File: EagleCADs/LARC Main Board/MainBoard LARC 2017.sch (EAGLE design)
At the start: 31 parts, among them IC1 7805TV

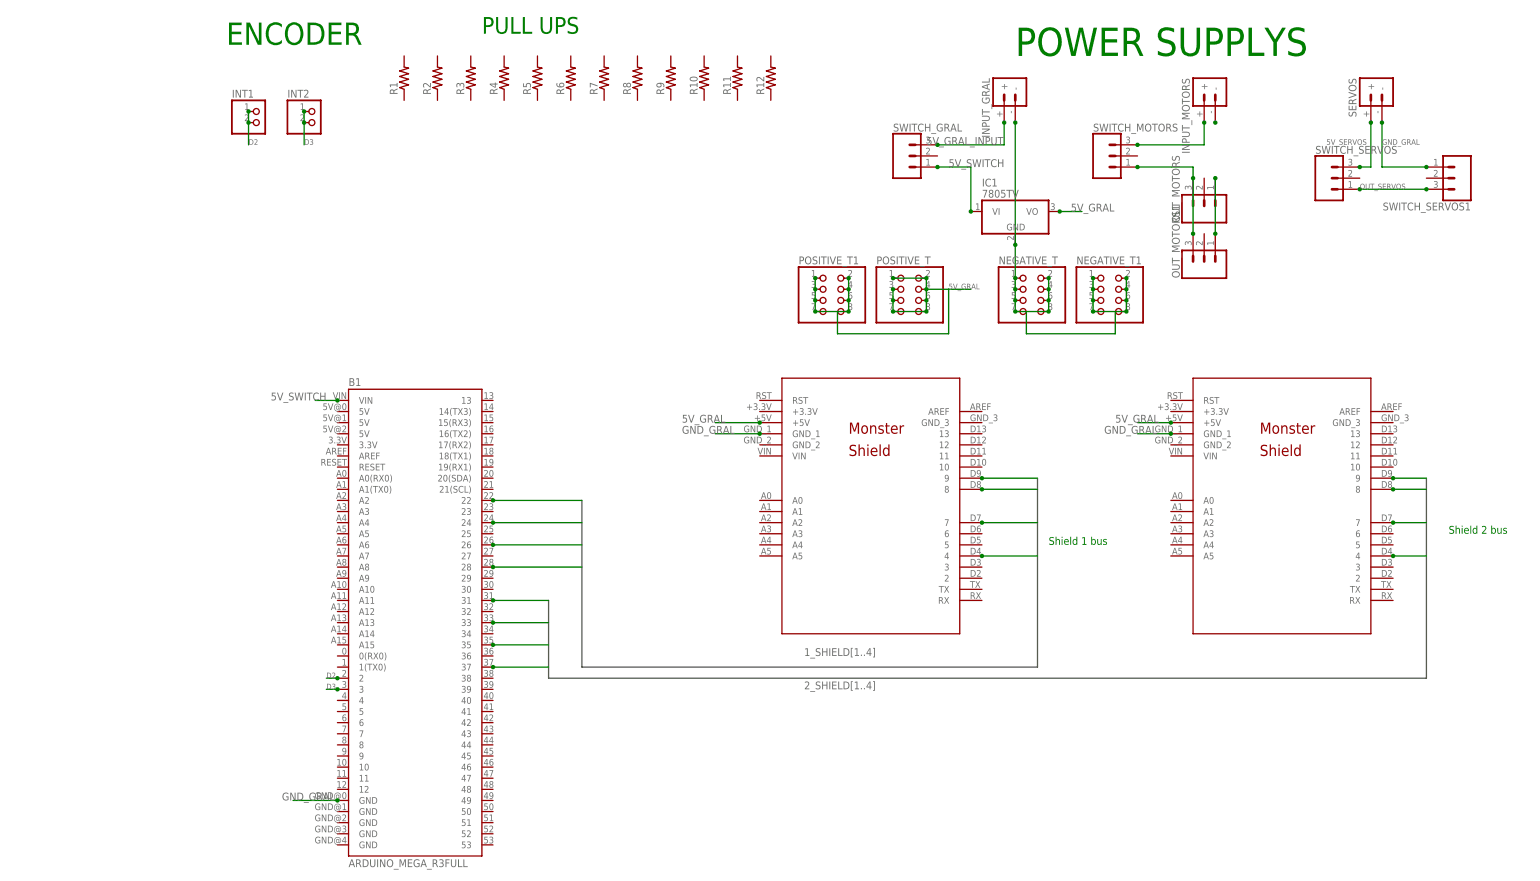
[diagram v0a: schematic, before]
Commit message: PCB Lower level finished
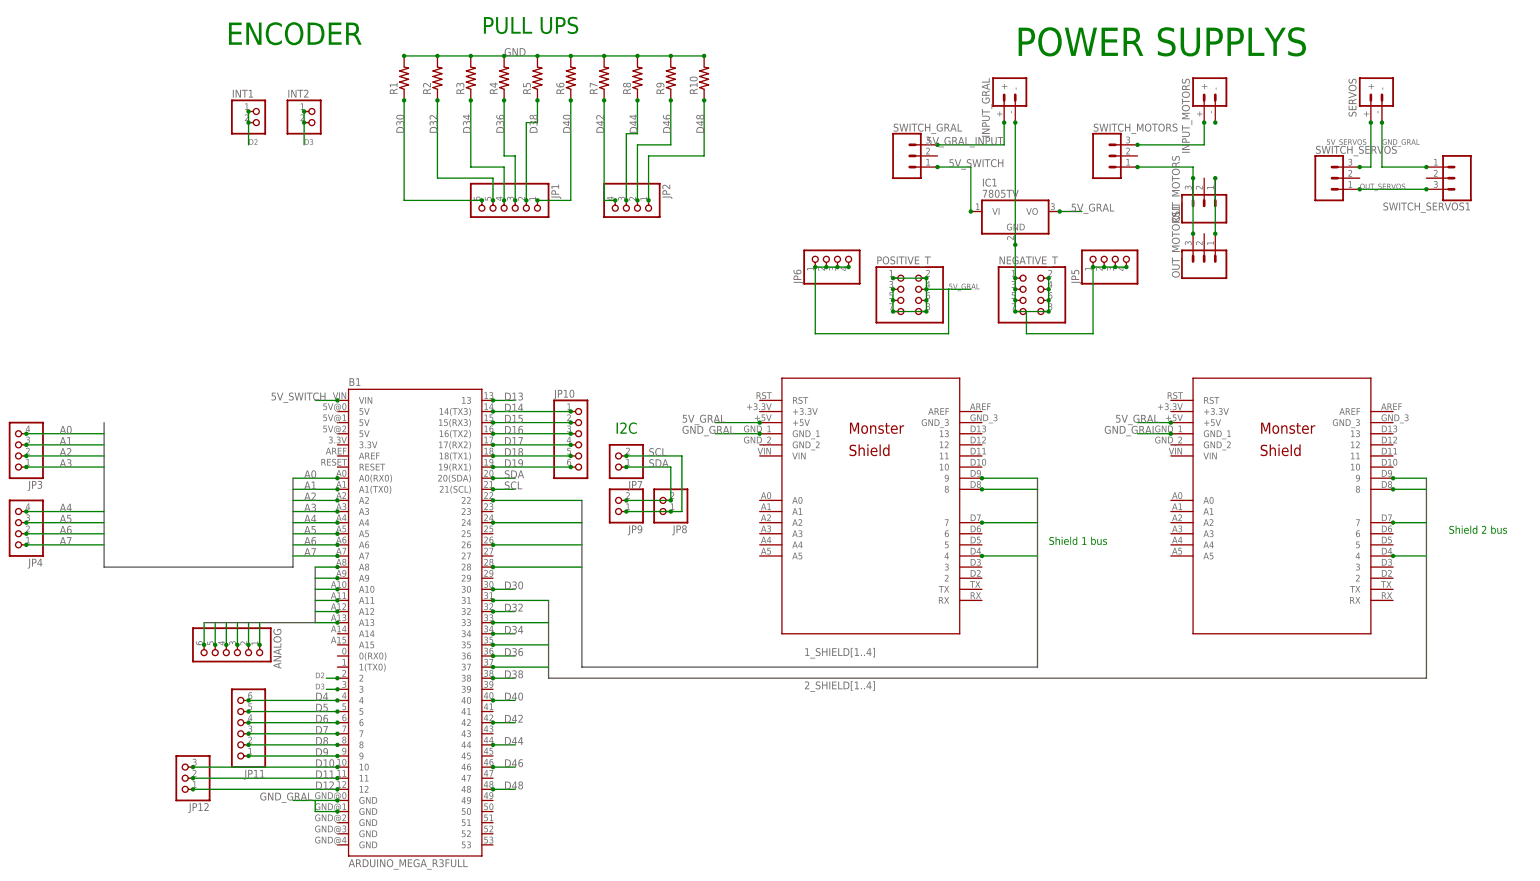
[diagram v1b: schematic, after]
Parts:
- removed NEGATIVE_T1, POSITIVE_T1: (no value), adafruit:PINHD-2X4
- removed R11, R12: (no value), adafruit:R-US_0207/9
- added ANALOG, JP1, JP10, JP11: (no value), pinhead:PINHD-1X6
- added JP12: (no value), pinhead:PINHD-1X3
- added JP2, JP3, JP4, JP5, JP6: (no value), pinhead:PINHD-1X4
- added JP7, JP8, JP9: (no value), pinhead:PINHD-1X2
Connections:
- new net A0: B1.A0(RX0), JP3.4
- new net A1: B1.A1(TX0), JP3.3
- new net A2: B1.A2, JP3.2
- new net A3: B1.A3, JP3.1
- new net A4: B1.A4, JP4.4
- new net A5: B1.A5, JP4.3
- new net A6: B1.A6, JP4.2
- new net A7: B1.A7, JP4.1
- new net ANALOGS10: ANALOG.4, B1.A10
- new net ANALOGS11: ANALOG.3, B1.A11
- new net ANALOGS12: ANALOG.2, B1.A12
- new net ANALOGS13: ANALOG.1, B1.A13
- new net ANALOGS8: ANALOG.6, B1.A8
- new net ANALOGS9: ANALOG.5, B1.A9
- new net D10: B1.10, JP12.3
- new net D11: B1.11, JP12.2
- new net D12: B1.12, JP12.1
- new net D13: B1.13
- new net D14: B1.14(TX3), JP10.1
- new net D15: B1.15(RX3), JP10.2
- new net D16: B1.16(TX2), JP10.3
- new net D17: B1.17(RX2), JP10.4
- new net D18: B1.18(TX1), JP10.5
- new net D19: B1.19(RX1), JP10.6
- new net D30: B1.30, JP1.6, R1.1
- new net D32: B1.32, JP1.5, R2.1
- new net D34: B1.34, JP1.4, R3.1
- new net D36: B1.36, JP1.3, R4.1
- new net D38: B1.38, JP1.2, R5.1
- new net D4: B1.4, JP11.6
- new net D40: B1.40, JP1.1, R6.1
- new net D42: B1.42, JP2.4, R7.1
- new net D44: B1.44, JP2.3, R8.1
- new net D46: B1.46, JP2.2, R9.1
- new net D48: B1.48, JP2.1, R10.1
- new net D5: B1.5, JP11.5
- new net D6: B1.6, JP11.4
- new net D7: B1.7, JP11.3
- new net D8: B1.8, JP11.2
- new net D9: B1.9, JP11.1
- new net GND: R1.2, R10.2, R2.2, R3.2, R4.2, R5.2, R6.2, R7.2, R8.2, R9.2
- new net SCL: B1.21(SCL), JP7.2, JP8.1, JP9.1
- new net SDA: B1.20(SDA), JP7.1, JP8.2, JP9.2
- net 5V_GRAL: now also JP6.1, JP6.2, JP6.3, JP6.4; no longer POSITIVE_T1.1, POSITIVE_T1.2, POSITIVE_T1.3, POSITIVE_T1.4, POSITIVE_T1.5, POSITIVE_T1.6, POSITIVE_T1.7, POSITIVE_T1.8
- net GND_GRAL: now also B1.GND@1, JP5.1, JP5.2, JP5.3, JP5.4; no longer NEGATIVE_T1.1, NEGATIVE_T1.2, NEGATIVE_T1.3, NEGATIVE_T1.4, NEGATIVE_T1.5, NEGATIVE_T1.6, NEGATIVE_T1.7, NEGATIVE_T1.8
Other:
- note added: "I2C"

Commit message: updates to the PCB
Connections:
- removed net GND: R1.2, R10.2, R2.2, R3.2, R4.2, R5.2, R6.2, R7.2, R8.2, R9.2
- net GND_GRAL: now also R1.2, R10.2, R2.2, R3.2, R4.2, R5.2, R6.2, R7.2, R8.2, R9.2
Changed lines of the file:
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@@
 <wire x1="284.48" y1="154.94" x2="294.64" y2="154.94" width="0.1524" layer="91"/>
+</segment>
+<segment>
+<pinref part="R1" gate="G$1" pin="2"/>
+<junction x="60.96" y="180.34"/>
+<pinref part="R2" gate="G$1" pin="2"/>
+<junction x="68.58" y="180.34"/>
+<wire x1="60.96" y1="180.34" x2="68.58" y2="180.34" width="0.1524" layer="91"/>
+<pinref part="R3" gate="G$1" pin="2"/>
+<junction x="76.2" y="180.34"/>
+<wire x1="68.58" y1="180.34" x2="76.2" y2="180.34" width="0.1524" layer="91"/>
+<pinref part="R4" gate="G$1" pin="2"/>
+<junction x="83.82" y="180.34"/>
+<wire x1="76.2" y1="180.34" x2="83.82" y2="180.34" width="0.1524" layer="91"/>
+<pinref part="R5" gate="G$1" pin="2"/>
+<junction x="91.44" y="180.34"/>
+<wire x1="83.82" y1="180.34" x2="91.44" y2="180.34" width="0.1524" layer="91"/>
+<label x="83.82" y="180.34" size="1.778" layer="95"/>
+<pinref part="R6" gate="G$1" pin="2"/>
+<junction x="99.06" y="180.34"/>
+<wire x1="91.44" y1="180.34" x2="99.06" y2="180.34" width="0.1524" layer="91"/>
+<pinref part="R7" gate="G$1" pin="2"/>
+<junction x="106.68" y="180.34"/>
+<wire x1="99.06" y1="180.34" x2="106.68" y2="180.34" width="0.1524" layer="91"/>
+<pinref part="R8" gate="G$1" pin="2"/>
+<junction x="114.3" y="180.34"/>
+<wire x1="106.68" y1="180.34" x2="114.3" y2="180.34" width="0.1524" layer="91"/>
+<pinref part="R9" gate="G$1" pin="2"/>
+<junction x="121.92" y="180.34"/>
+<wire x1="114.3" y1="180.34" x2="121.92" y2="180.34" width="0.1524" layer="91"/>
+<pinref part="R10" gate="G$1" pin="2"/>
+<junction x="129.54" y="180.34"/>
+<wire x1="121.92" y1="180.34" x2="129.54" y2="180.34" width="0.1524" layer="91"/>
 </segment>
 </net>
@@
 </segment>
 </net>
-<net name="GND" class="0">
-<segment>
-<pinref part="R1" gate="G$1" pin="2"/>
-<junction x="60.96" y="180.34"/>
-<pinref part="R2" gate="G$1" pin="2"/>
-<junction x="68.58" y="180.34"/>
-<wire x1="60.96" y1="180.34" x2="68.58" y2="180.34" width="0.1524" layer="91"/>
-<pinref part="R3" gate="G$1" pin="2"/>
-<junction x="76.2" y="180.34"/>
-<wire x1="68.58" y1="180.34" x2="76.2" y2="180.34" width="0.1524" layer="91"/>
-<pinref part="R4" gate="G$1" pin="2"/>
-<junction x="83.82" y="180.34"/>
-<wire x1="76.2" y1="180.34" x2="83.82" y2="180.34" width="0.1524" layer="91"/>
-<pinref part="R5" gate="G$1" pin="2"/>
-<junction x="91.44" y="180.34"/>
-<wire x1="83.82" y1="180.34" x2="91.44" y2="180.34" width="0.1524" layer="91"/>
-<label x="83.82" y="180.34" size="1.778" layer="95"/>
-<pinref part="R6" gate="G$1" pin="2"/>
-<junction x="99.06" y="180.34"/>
-<wire x1="91.44" y1="180.34" x2="99.06" y2="180.34" width="0.1524" layer="91"/>
-<pinref part="R7" gate="G$1" pin="2"/>
-<junction x="106.68" y="180.34"/>
-<wire x1="99.06" y1="180.34" x2="106.68" y2="180.34" width="0.1524" layer="91"/>
-<pinref part="R8" gate="G$1" pin="2"/>
-<junction x="114.3" y="180.34"/>
-<wire x1="106.68" y1="180.34" x2="114.3" y2="180.34" width="0.1524" layer="91"/>
-<pinref part="R9" gate="G$1" pin="2"/>
-<junction x="121.92" y="180.34"/>
-<wire x1="114.3" y1="180.34" x2="121.92" y2="180.34" width="0.1524" layer="91"/>
-<pinref part="R10" gate="G$1" pin="2"/>
-<junction x="129.54" y="180.34"/>
-<wire x1="121.92" y1="180.34" x2="129.54" y2="180.34" width="0.1524" layer="91"/>
-</segment>
-</net>

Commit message: MainBoard v1.0
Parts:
- added JP13: (no value), pinhead:PINHD-1X4
- JP11: device pinhead:PINHD-1X6 -> pinhead:PINHD-1X4
- JP12: device pinhead:PINHD-1X3 -> pinhead:PINHD-1X5
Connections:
- removed net D10: B1.10, JP12.3
- removed net D11: B1.11, JP12.2
- removed net D12: B1.12, JP12.1
- removed net D9: B1.9, JP11.1
- new net PWM1_M1: B1.12, MS_1.6
- new net PWM1_M2: B1.10, MS_2.5
- new net PWM2_M1: B1.11, MS_1.5
- new net PWM2_M2: B1.9, MS_2.6
- net 5V_GRAL: now also JP11.1, JP11.2, JP11.3, JP11.4
- net 5V_SWITCH: now also R1.2, R10.2, R2.2, R3.2, R4.2, R5.2, R6.2, R7.2, R8.2, R9.2
- net D4: now also JP12.5; no longer JP11.6
- net D5: now also JP12.4; no longer JP11.5
- net D6: now also JP12.3; no longer JP11.4
- net D7: now also JP12.2; no longer JP11.3
- net D8: now also JP12.1; no longer JP11.2
- net GND_GRAL: now also JP13.1, JP13.2, JP13.3, JP13.4; no longer R1.2, R10.2, R2.2, R3.2, R4.2, R5.2, R6.2, R7.2, R8.2, R9.2
